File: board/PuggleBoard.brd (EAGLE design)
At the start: 54.6 x 86.4 mm, 136 parts, among them U1 OPA365, U10 AD5686, U11 LM2663, U12 MAX1735, U13 TLV70245, U14 REF5040, U15 AD8032, U16 24C, U2 OPA365, U3 OPA365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

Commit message: Fixed the ribbon cable mapping to take into account reflective symmetry.
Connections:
- new net N$17: BB1.27
- new net N$25: BB1.29
- new net N$26: BB1.30
- new net N$27: BB1.28
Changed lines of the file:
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@@
 <wire x1="22.943109375" y1="44.45" x2="23.495" y2="44.2214" width="0.254" layer="1" curve="-45"/>
+</signal>
+<signal name="N$17">
+<contactref element="BB1" pad="27"/>
+</signal>
+<signal name="N$25">
+<contactref element="BB1" pad="29"/>
+</signal>
+<signal name="N$26">
+<contactref element="BB1" pad="30"/>
+</signal>
+<signal name="N$27">
+<contactref element="BB1" pad="28"/>
 </signal>
 </signals>

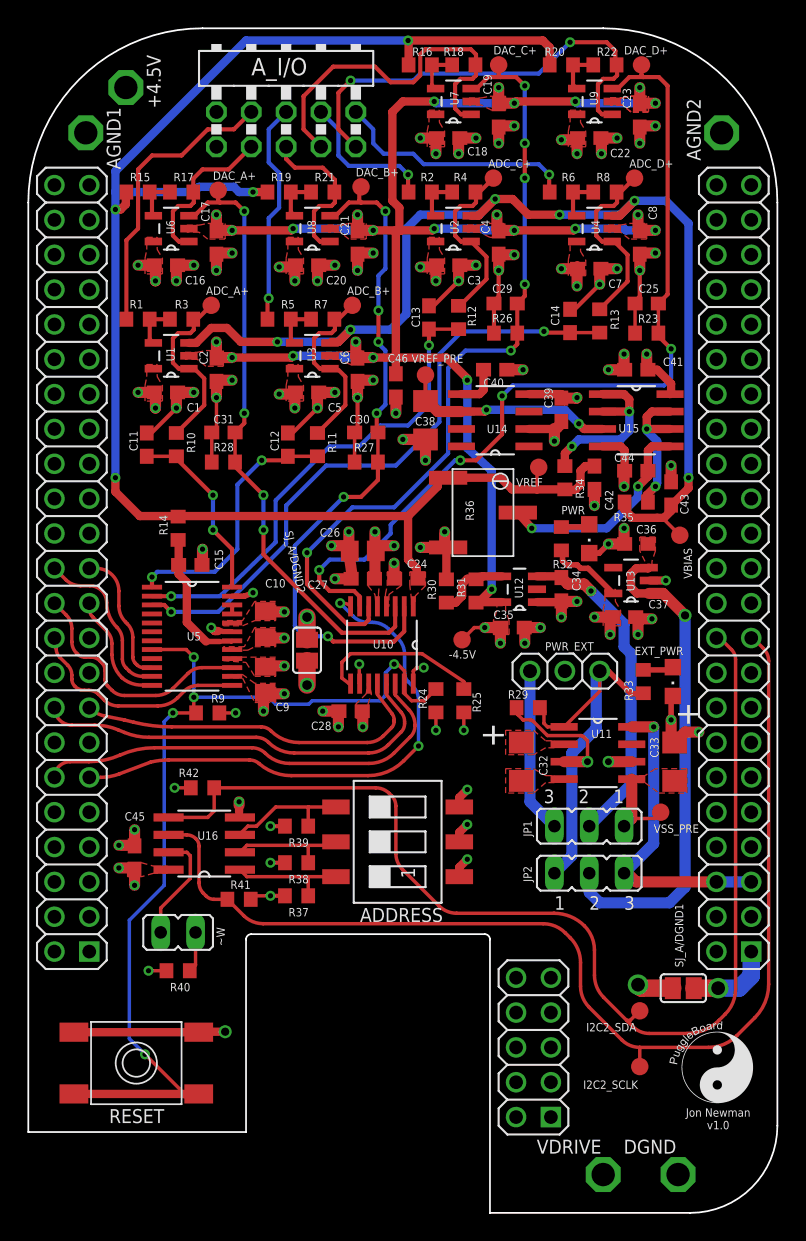
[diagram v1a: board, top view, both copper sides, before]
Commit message: Fixed the GPIO pin out to match pins available to the PRU in MODE6
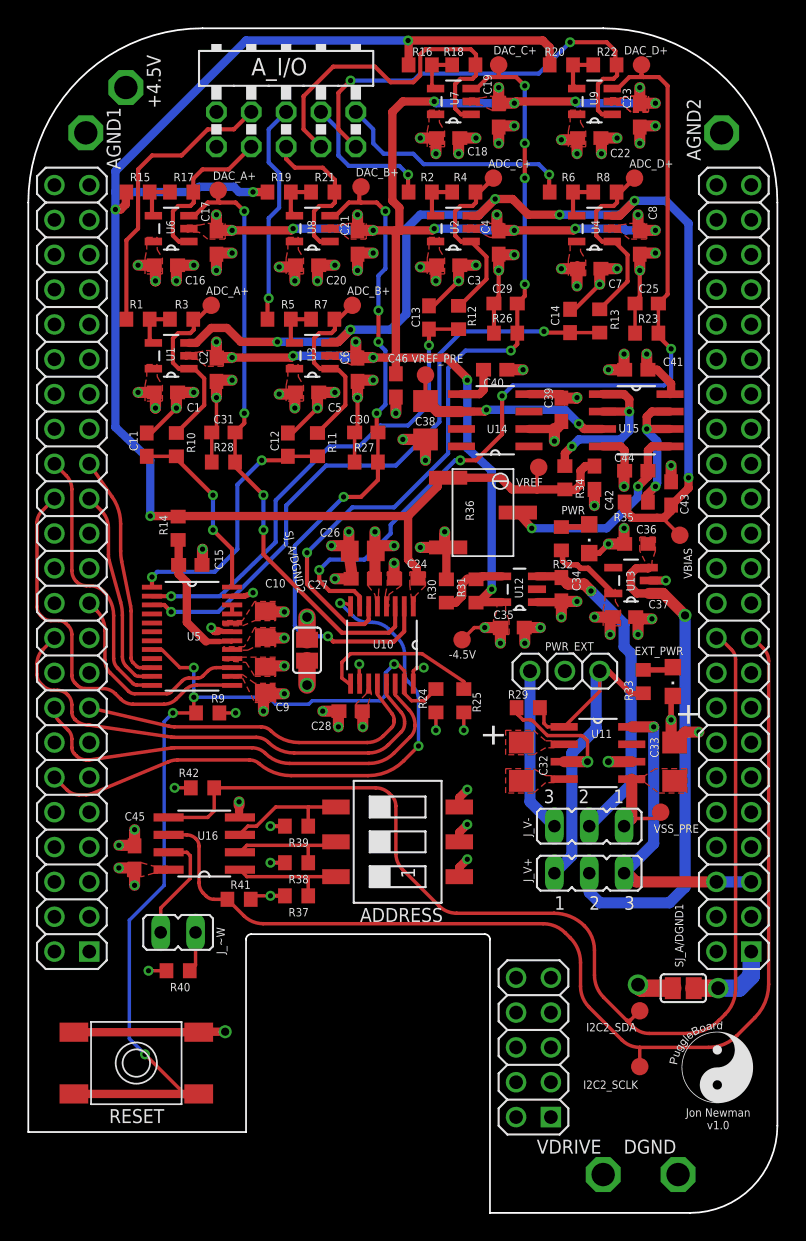
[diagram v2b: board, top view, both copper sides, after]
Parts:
- renumbered JP1 to J_V-, JP2 to J_V+, ~W to J_~W
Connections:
- removed net N$17: BB1.27
- removed net N$25: BB1.29
- removed net N$26: BB1.30
- removed net N$27: BB1.28
- net ADC_SPI0: now also BB1.29; no longer BB1.23
- net ADC_SPI1: now also BB1.27; no longer BB1.24
- net ADC_SPI2: now also BB1.30; no longer BB1.21
- net ADC_SPI3: now also BB1.28; no longer BB1.20
- net ADC_SPI4: now also BB1.21; no longer BB1.22
- net DAC_SPI1: now also BB1.20; no longer BB1.16
- net DAC_SPI2: now also BB1.16; no longer BB1.12
- net DAC_SPI3: now also BB1.12; no longer BB1.11
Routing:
- net ADC_SPI3: track 16.2 -> 28.4 mm
- net ADC_SPI2: track 8.42 -> 20.0 mm
- net ADC_SPI0: track 9.68 -> 16.7 mm
- net DAC_SPI1: track 30.7 -> 36.6 mm
- net DAC_SPI3: track 39.2 -> 42.5 mm
- net ADC_SPI1: track 11.8 -> 15.0 mm
- net ADC_SPI4: track 17.9 -> 15.6 mm
- net DAC_SPI2: track 31.8 -> 33.8 mm

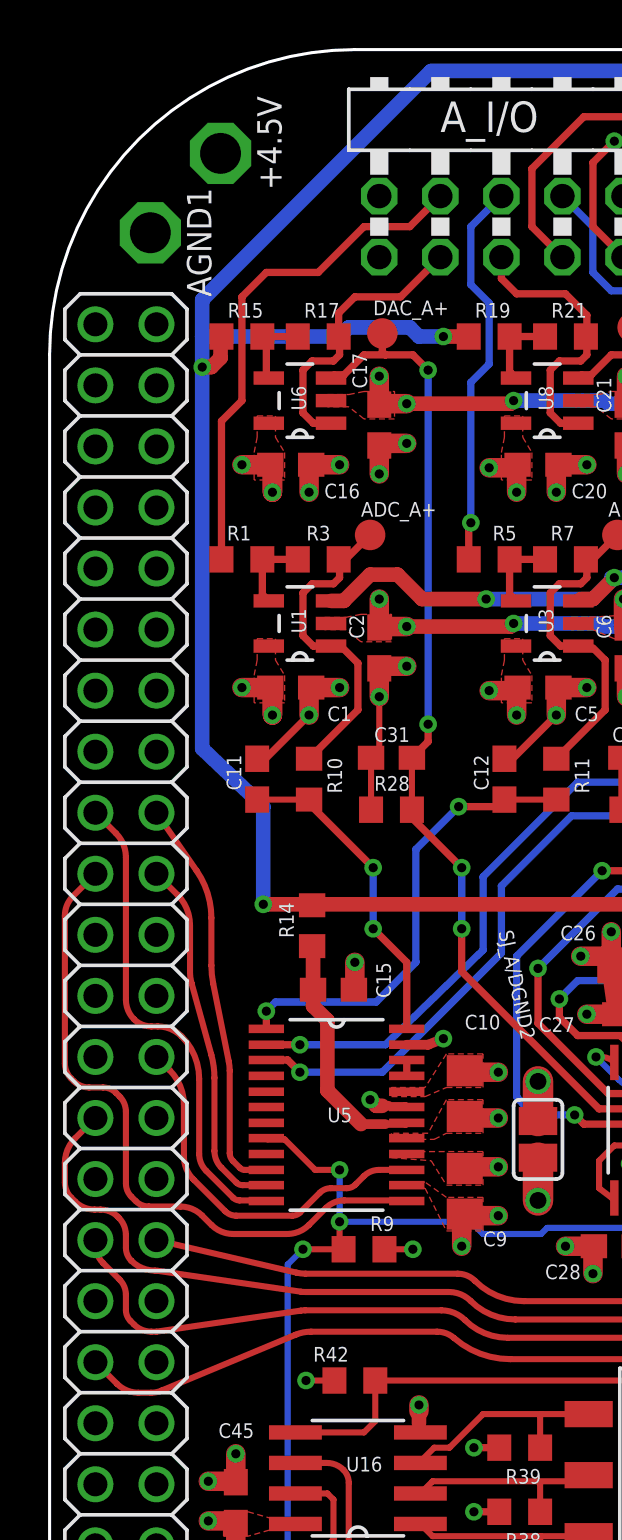
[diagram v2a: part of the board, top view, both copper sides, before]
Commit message: Almost done actually fixing GPIO mapping for PRU1
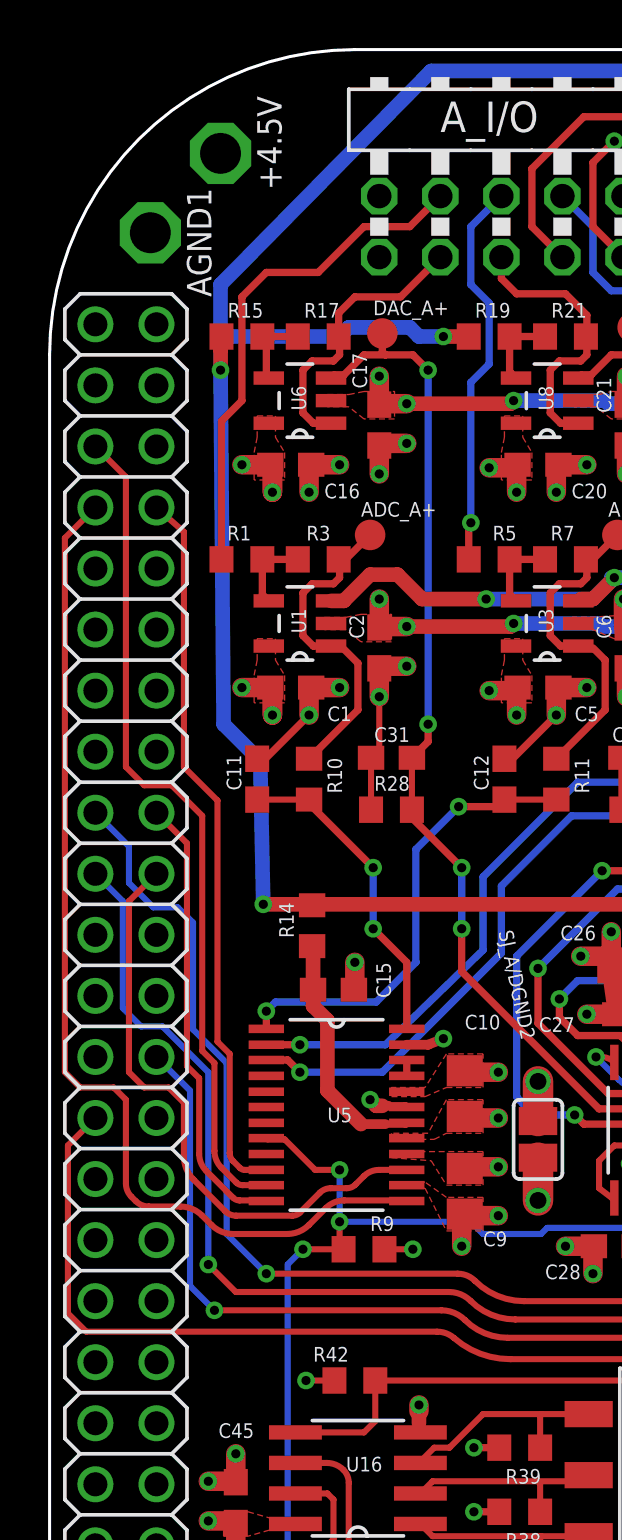
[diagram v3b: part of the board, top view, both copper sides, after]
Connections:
- net ADC_SPI0: now also BB1.39; no longer BB1.29
- net ADC_SPI1: now also BB1.42; no longer BB1.27
- net ADC_SPI2: now also BB1.29; no longer BB1.30
- net ADC_SPI3: now also BB1.40; no longer BB1.28
- net ADC_SPI4: now also BB1.27; no longer BB1.21
- net DAC_SPI0: now also BB1.30; no longer BB1.15
- net DAC_SPI1: now also BB1.28; no longer BB1.20
- net DAC_SPI2: now also BB1.21; no longer BB1.16
- net DAC_SPI3: now also BB1.20; no longer BB1.12
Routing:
- net ADC_SPI1: track 15.0 -> 34.9 mm
- net DAC_SPI0: track 26.4 -> 44.4 mm, vias 0 -> 1
- net ADC_SPI3: track 28.4 -> 44.0 mm
- net ADC_SPI0: track 16.7 -> 30.0 mm
- net ADC_SPI4: track 15.6 -> 24.9 mm
- net DAC_SPI3: track 42.5 -> 51.6 mm
- net DAC_SPI1: track 36.6 -> 44.6 mm, vias 0 -> 1
- net DAC_SPI2: track 33.8 -> 37.8 mm, vias 0 -> 1
- net VREF: track 120.5 -> 118.5 mm
- net ADC_SPI2: track 20.0 -> 18.7 mm

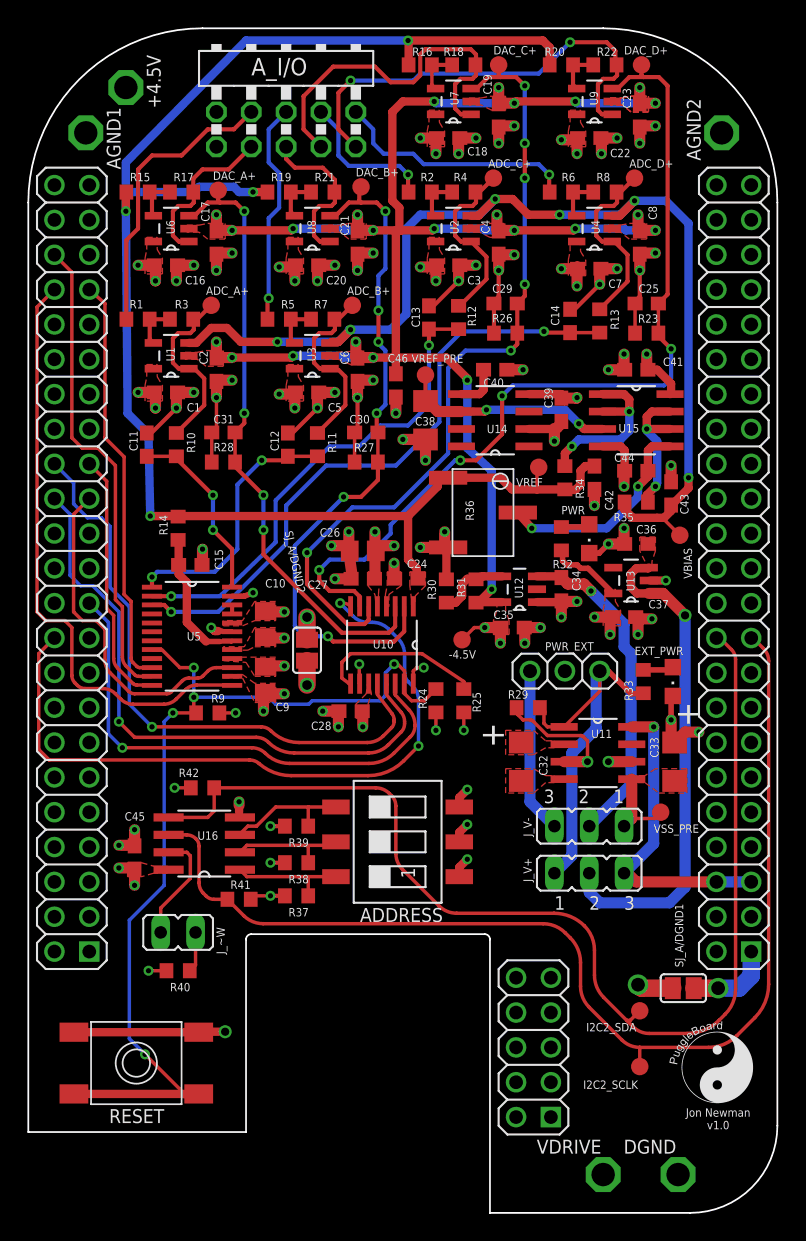
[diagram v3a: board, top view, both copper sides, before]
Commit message: Routed the SPI busses to GPIO pins accessible by PRU1.
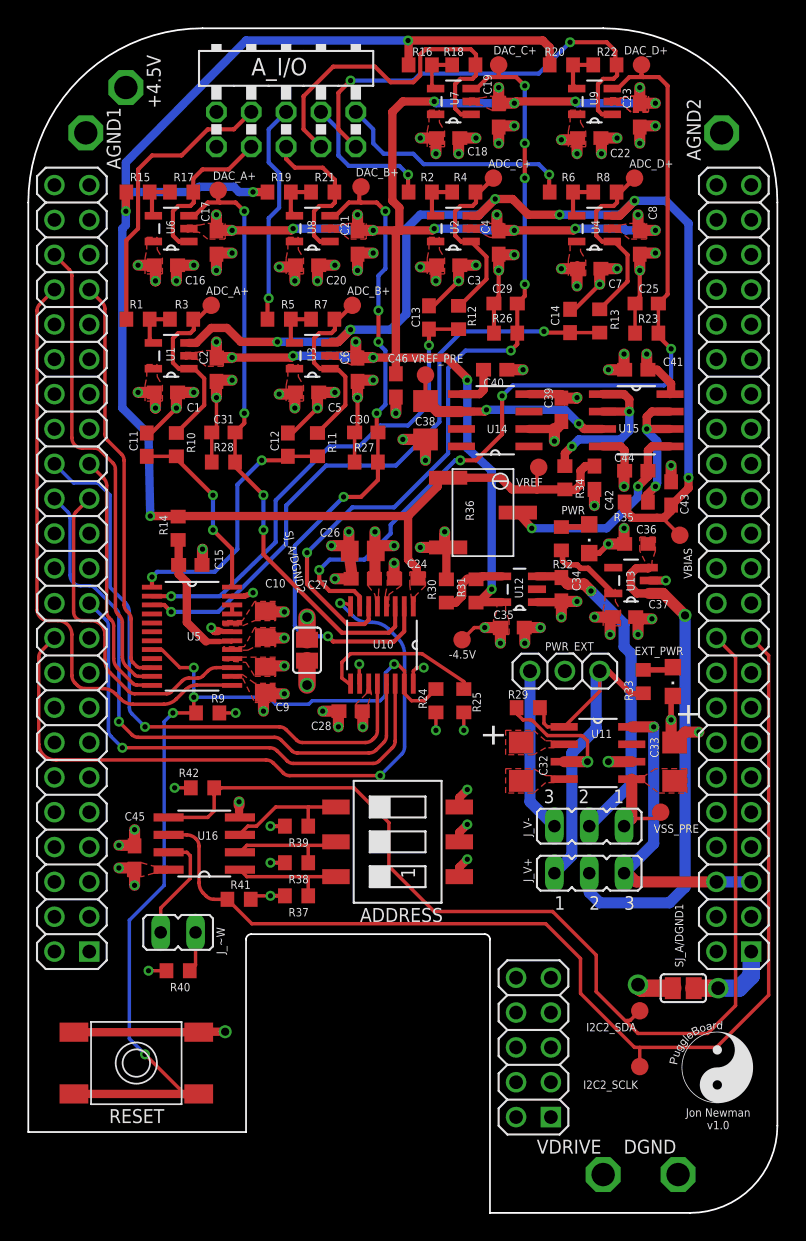
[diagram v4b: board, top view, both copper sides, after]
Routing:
- net DAC_SPI1: track 44.6 -> 43.4 mm
- net DAC_SPI2: track 37.8 -> 36.7 mm
- net DAC_SPI3: track 51.6 -> 50.6 mm

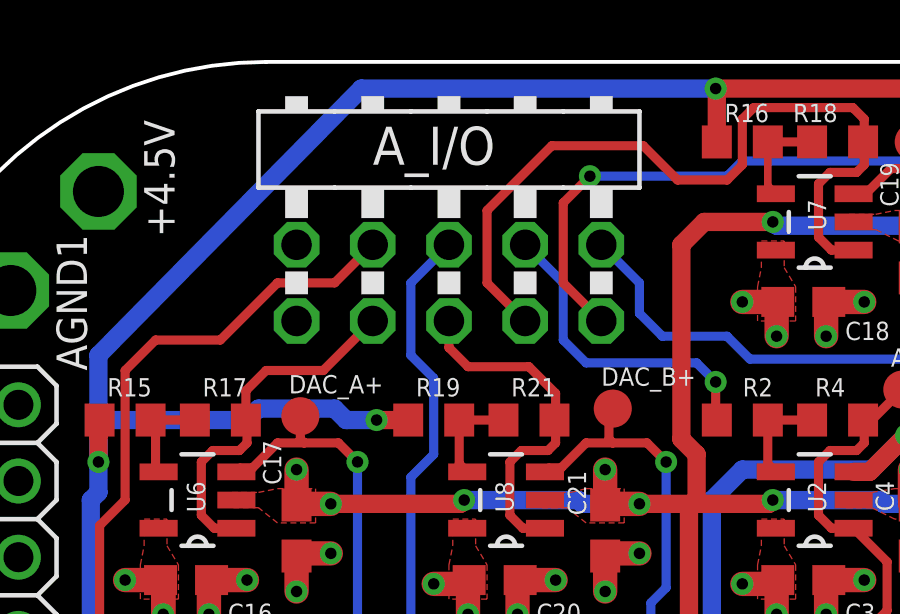
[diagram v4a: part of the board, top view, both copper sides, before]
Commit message: Silkscreen changes.
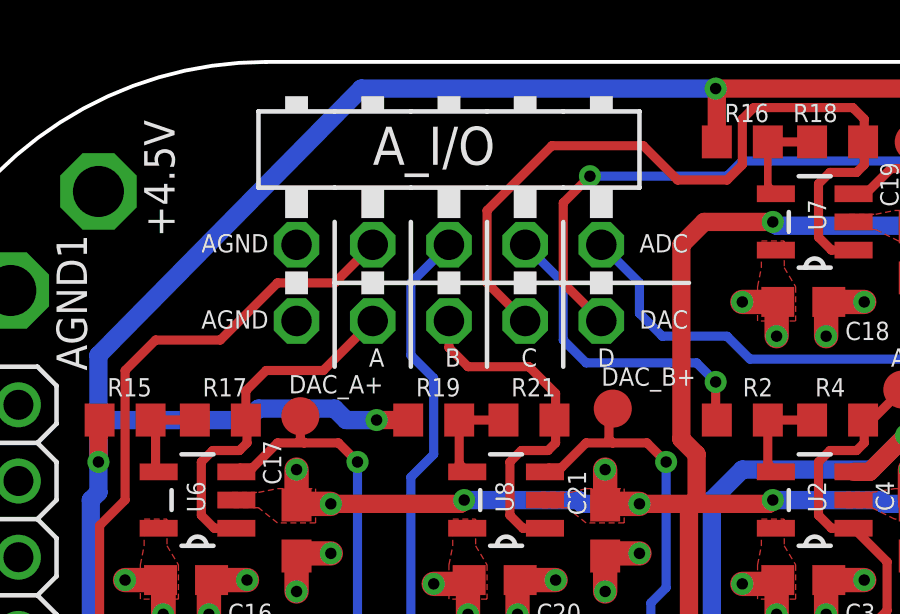
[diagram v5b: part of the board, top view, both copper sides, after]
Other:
- board text added: "A"
- board text added: "ADC"
- board text added: "AGND"
- board text added: "B"
- board text added: "C"
- board text added: "D"
- board text added: "DAC"
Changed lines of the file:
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@@
 <layers>
 <layer number="1" name="Top" color="4" fill="1" visible="yes" active="yes"/>
-<layer number="2" name="Route2" color="1" fill="3" visible="yes" active="yes"/>
+<layer number="2" name="Route2" color="1" fill="3" visible="no" active="yes"/>
 <layer number="3" name="Route3" color="4" fill="3" visible="no" active="no"/>
 <layer number="4" name="Route4" color="1" fill="4" visible="no" active="no"/>
@@
 <layer number="13" name="Route13" color="4" fill="5" visible="no" active="no"/>
 <layer number="14" name="Route14" color="1" fill="6" visible="no" active="no"/>
-<layer number="15" name="Route15" color="4" fill="6" visible="yes" active="yes"/>
+<layer number="15" name="Route15" color="4" fill="6" visible="no" active="yes"/>
 <layer number="16" name="Bottom" color="1" fill="1" visible="yes" active="yes"/>
 <layer number="17" name="Pads" color="2" fill="1" visible="yes" active="yes"/>
@@
 <layer number="19" name="Unrouted" color="6" fill="1" visible="yes" active="yes"/>
 <layer number="20" name="Dimension" color="15" fill="1" visible="yes" active="yes"/>
-<layer number="21" name="tPlace" color="7" fill="1" visible="no" active="yes"/>
+<layer number="21" name="tPlace" color="7" fill="1" visible="yes" active="yes"/>
 <layer number="22" name="bPlace" color="7" fill="1" visible="no" active="yes"/>
 <layer number="23" name="tOrigins" color="15" fill="1" visible="yes" active="yes"/>
@@
 <text x="50.292" y="6.858" size="0.6096" layer="21" font="vector" align="center">Jon Newman
 v1.0</text>
+<text x="10.541" y="80.01" size="0.6096" layer="21" font="vector">AGND</text>
+<text x="10.541" y="77.47" size="0.6096" layer="21" font="vector">AGND</text>
+<text x="25.146" y="80.01" size="0.6096" layer="21" font="vector">ADC</text>
+<text x="25.146" y="77.47" size="0.6096" layer="21" font="vector">DAC</text>
+<text x="23.749" y="76.2" size="0.6096" layer="21" font="vector">D</text>
+<text x="21.209" y="76.2" size="0.6096" layer="21" font="vector">C</text>
+<text x="18.669" y="76.2" size="0.6096" layer="21" font="vector">B</text>
+<text x="16.129" y="76.2" size="0.6096" layer="21" font="vector">A</text>
+<wire x1="14.986" y1="78.994" x2="26.797" y2="78.994" width="0.1524" layer="21"/>
+<wire x1="17.526" y1="81.026" x2="17.526" y2="76.2" width="0.1524" layer="21"/>
+<wire x1="20.066" y1="81.026" x2="20.066" y2="76.2" width="0.1524" layer="21"/>
+<wire x1="22.606" y1="81.026" x2="22.606" y2="76.2" width="0.1524" layer="21"/>
+<wire x1="14.986" y1="81.026" x2="14.986" y2="76.2" width="0.1524" layer="21"/>
 </plain>
 <attributes>

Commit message: Minor.
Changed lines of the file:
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@@
 <wire x1="13.081" y1="28.829" x2="10.227" y2="28.829" width="0.254" layer="1"/>
 <wire x1="51.562" y1="40.513" x2="51.562" y2="15.113" width="0.254" layer="1"/>
-<wire x1="44.577" y1="14.732" x2="43.8785" y2="14.0335" width="0.254" layer="1"/>
-<wire x1="43.8785" y1="14.0335" x2="43.6245" y2="14.0335" width="0.254" layer="1"/>
+<wire x1="44.577" y1="14.732" x2="43.7515" y2="13.9065" width="0.254" layer="1"/>
 <wire x1="51.562" y1="15.113" x2="49.53" y2="13.081" width="0.254" layer="1"/>
 <wire x1="49.53" y1="13.081" x2="44.45" y2="13.081" width="0.254" layer="1"/>
-<wire x1="44.45" y1="13.081" x2="41.402" y2="16.129" width="0.254" layer="1"/>
+<wire x1="44.45" y1="13.081" x2="43.6245" y2="13.9065" width="0.254" layer="1"/>
+<wire x1="43.6245" y1="13.9065" x2="41.402" y2="16.129" width="0.254" layer="1"/>
 <wire x1="41.402" y1="16.129" x2="41.402" y2="18.796" width="0.254" layer="1"/>
-<wire x1="41.402" y1="18.796" x2="38.227" y2="21.971" width="0.254" layer="1"/>
-<wire x1="38.227" y1="21.971" x2="29.591" y2="21.971" width="0.254" layer="1"/>
-<wire x1="29.591" y1="21.971" x2="26.289" y2="25.273" width="0.254" layer="1"/>
+<wire x1="41.402" y1="18.796" x2="38.1" y2="22.098" width="0.254" layer="1"/>
+<wire x1="38.1" y1="22.098" x2="29.464" y2="22.098" width="0.254" layer="1"/>
+<wire x1="29.464" y1="22.098" x2="26.289" y2="25.273" width="0.254" layer="1"/>
 <wire x1="26.289" y1="25.273" x2="26.289" y2="28.448" width="0.254" layer="1"/>
 <wire x1="26.289" y1="28.448" x2="23.749" y2="30.988" width="0.254" layer="1"/>
@@
 <wire x1="14.058" y1="30.988" x2="13.55" y2="30.48" width="0.254" layer="1"/>
 <wire x1="51.562" y1="40.513" x2="50.165" y2="41.91" width="0.254" layer="1"/>
-<wire x1="44.45" y1="13.081" x2="43.8785" y2="14.0335" width="0" layer="19" extent="1-1"/>
+<wire x1="43.7515" y1="13.9065" x2="43.6245" y2="13.9065" width="0.254" layer="1"/>
 </signal>
 <signal name="N$14">
